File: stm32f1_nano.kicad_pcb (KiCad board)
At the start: 2 copper layers, 43.2 x 17.8 mm, 45 parts, among them J1 Analog, J2 Digital, J3 TYPE-C-31-M-12, J5 DEBUG, U1 STM32F103C8T6, U2 SST26VF016BEUI-104I/SN, U4 XC6206P332MR, U5 AMS1117-5.0, Y1 X322516MLB4SI

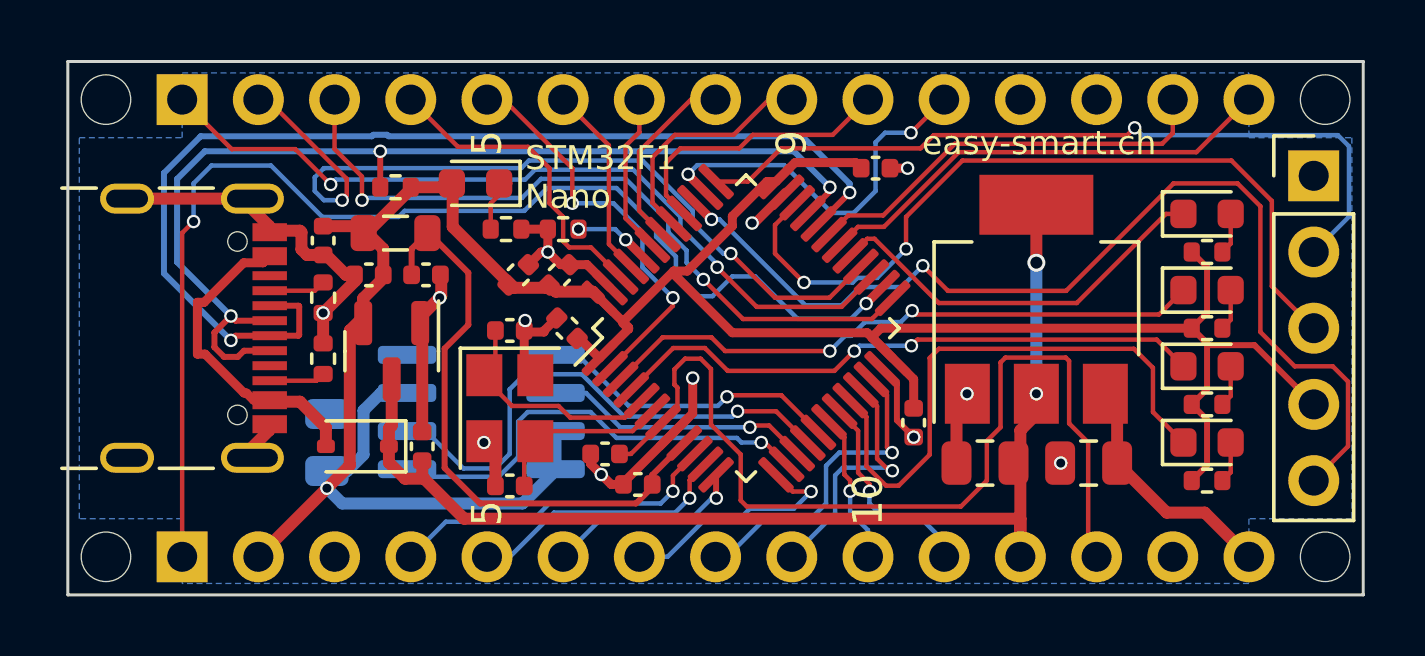
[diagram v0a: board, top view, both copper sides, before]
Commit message: #12 Add pin description to front
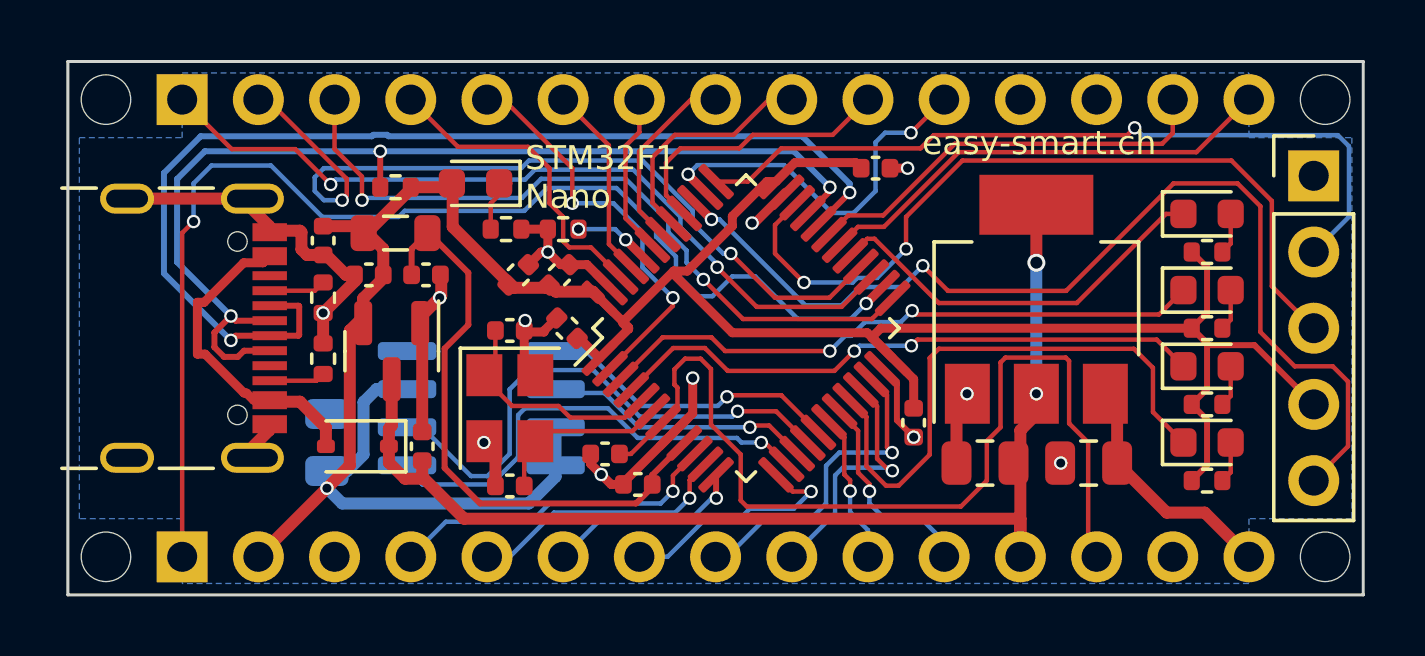
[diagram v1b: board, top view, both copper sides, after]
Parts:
- moved U2 0.13 mm to (113.8, 93.8)
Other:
- board text removed: "10"
- board text removed: "5"
- board text removed: "9"

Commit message: #12 Add pin description to front
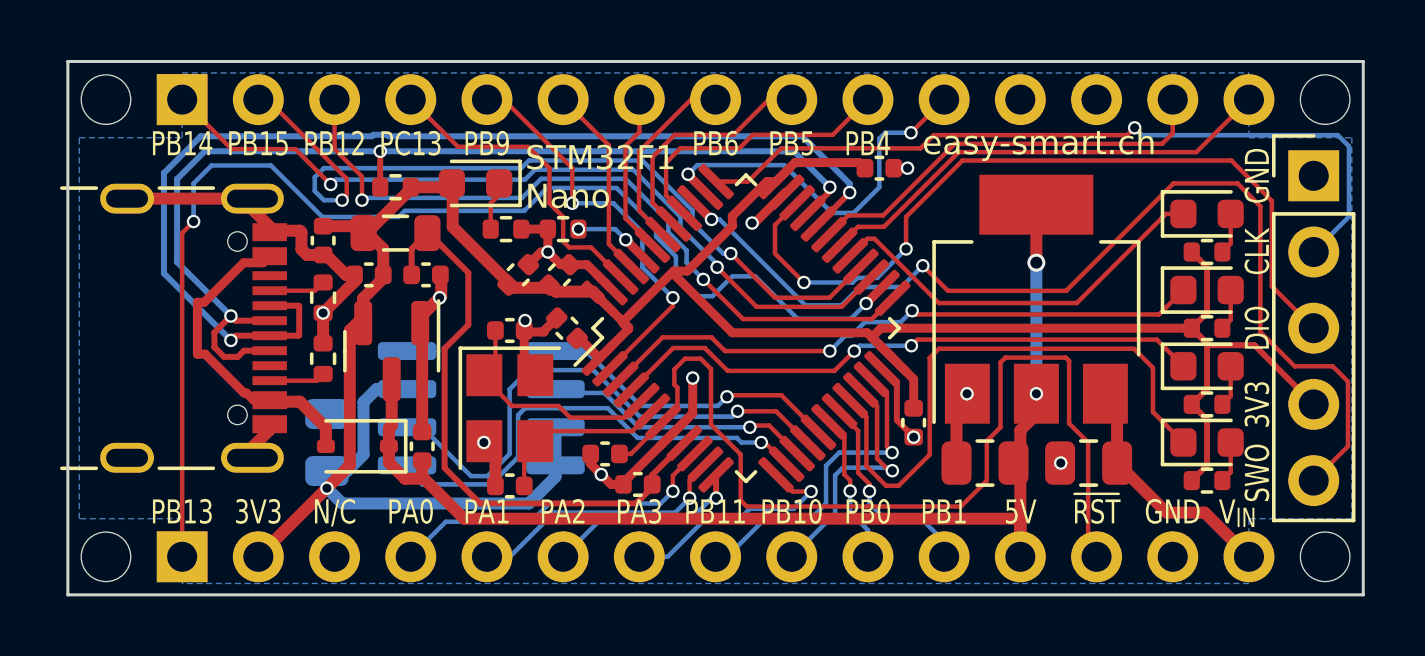
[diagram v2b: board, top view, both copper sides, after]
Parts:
- added G***: LOGO, #Logo:e-Logo 5mm, B.Cu at (123.6, 91.1)
- moved C3 0.13 mm to (127.1, 85.8)
